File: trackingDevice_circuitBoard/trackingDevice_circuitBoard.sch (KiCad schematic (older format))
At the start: 17 parts, among them P1 Digital, P2 COM, P4 Analog, Q1 Q_NPN_EBC, Q2 Q_NPN_EBC, Q3 Q_NPN_EBC, U1 HC-12, U2 GY-NEO6MV2, U3 TP4056

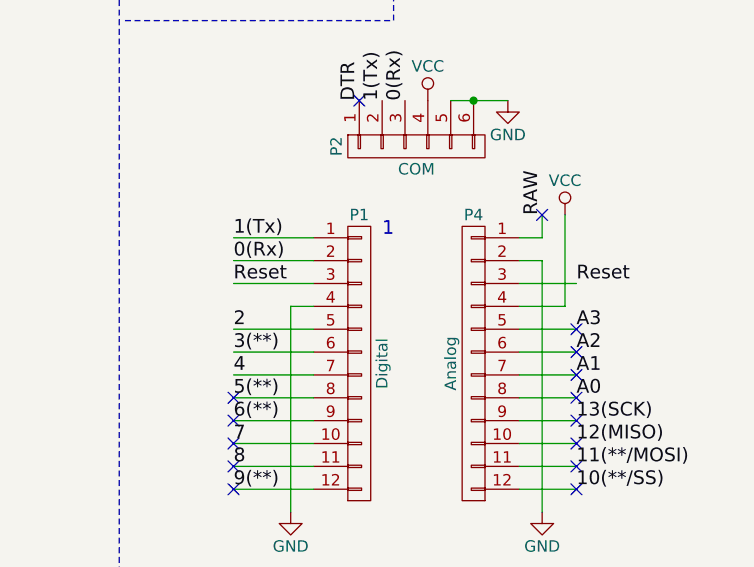
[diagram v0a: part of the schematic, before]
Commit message: Added veroboard/stripboard drill marks + corrected error in tracking device circuit
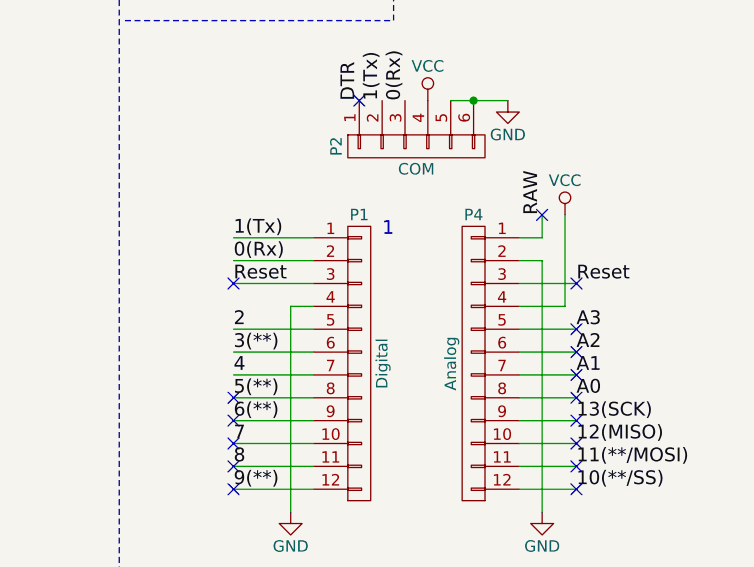
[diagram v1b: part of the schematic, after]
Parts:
- Q1: footprint TO_SOT_Packages_THT:TO-126_Vertical -> TO_SOT_Packages_THT:TO-92_Inline_Wide
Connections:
- no-connect marks 16 -> 18
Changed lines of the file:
@@
 Sheet 1 1
 Title "Arduino GPS Tracker - Tracking Device"
-Date "2018-07-16"
+Date "2018-08-09"
 Rev "1"
 Comp "By Megasaturnv"
@@
 F 0 "Q1" H 4500 2350 50  0000 L CNN
 F 1 "Q_NPN_EBC" H 4500 2250 50  0000 L CNN
-F 2 "TO_SOT_Packages_THT:TO-126_Vertical" H 4500 2400 50  0001 C CNN
+F 2 "TO_SOT_Packages_THT:TO-92_Inline_Wide" H 4500 2400 50  0001 C CNN
 F 3 "" H 4300 2300 50  0001 C CNN
 	1    4300 2300
@@
 	1    0    0    -1
 $EndComp
+NoConn ~ 10500 1800
+NoConn ~ 9000 1800
 $EndSCHEMATC

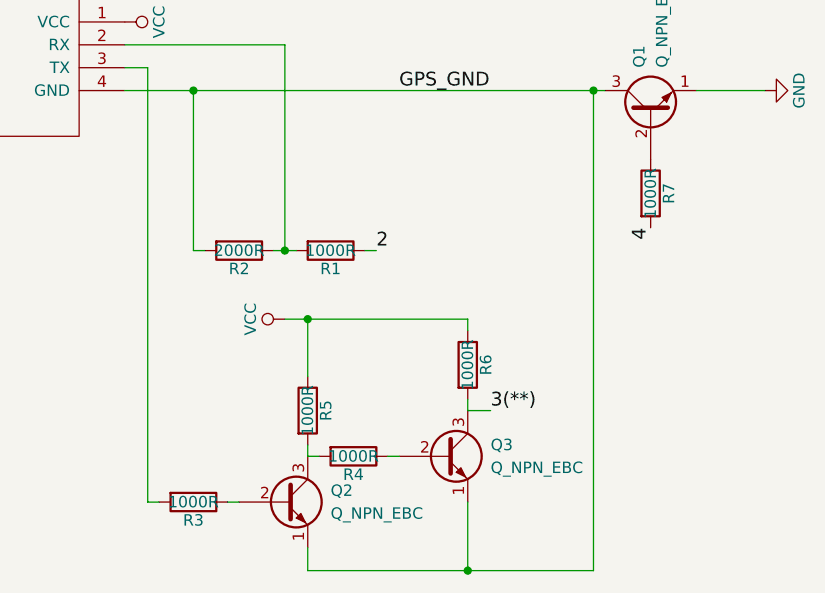
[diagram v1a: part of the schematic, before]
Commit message: Modified resistor values to be more power-efficient
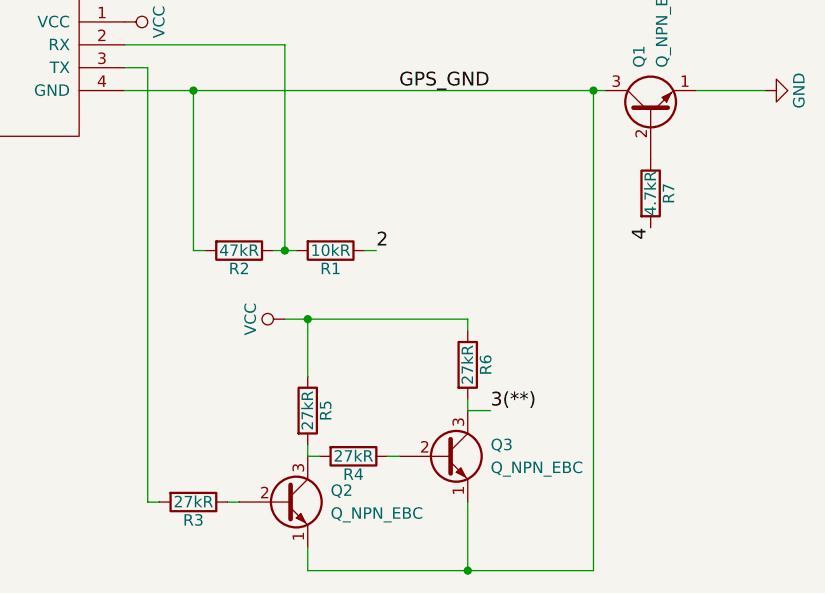
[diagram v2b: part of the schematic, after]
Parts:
- R1: value 1000R -> 10kR
- R2: value 2000R -> 47kR
- R3, R4, R5, R6: value 1000R -> 27kR
- R7: value 1000R -> 4.7kR
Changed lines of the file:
@@
 Sheet 1 1
 Title "Arduino GPS Tracker - Tracking Device"
-Date "2018-08-09"
+Date "2018-08-10"
 Rev "1"
 Comp "By Megasaturnv"
@@
 P 2900 2900
 F 0 "R1" V 2980 2900 50  0000 C CNN
-F 1 "1000R" V 2900 2900 50  0000 C CNN
+F 1 "10kR" V 2900 2900 50  0000 C CNN
 F 2 "Resistors_THT:R_Axial_DIN0207_L6.3mm_D2.5mm_P10.16mm_Horizontal" V 2830 2900 50  0001 C CNN
 F 3 "" H 2900 2900 50  0001 C CNN
@@
 P 2500 2900
 F 0 "R2" V 2580 2900 50  0000 C CNN
-F 1 "2000R" V 2500 2900 50  0000 C CNN
+F 1 "47kR" V 2500 2900 50  0000 C CNN
 F 2 "Resistors_THT:R_Axial_DIN0207_L6.3mm_D2.5mm_P10.16mm_Horizontal" V 2430 2900 50  0001 C CNN
 F 3 "" H 2500 2900 50  0001 C CNN
@@
 P 2300 4000
 F 0 "R3" V 2380 4000 50  0000 C CNN
-F 1 "1000R" V 2300 4000 50  0000 C CNN
+F 1 "27kR" V 2300 4000 50  0000 C CNN
 F 2 "Resistors_THT:R_Axial_DIN0207_L6.3mm_D2.5mm_P10.16mm_Horizontal" V 2230 4000 50  0001 C CNN
 F 3 "" H 2300 4000 50  0001 C CNN
@@
 P 3000 3800
 F 0 "R4" V 3080 3800 50  0000 C CNN
-F 1 "1000R" V 3000 3800 50  0000 C CNN
+F 1 "27kR" V 3000 3800 50  0000 C CNN
 F 2 "Resistors_THT:R_Axial_DIN0207_L6.3mm_D2.5mm_P10.16mm_Horizontal" V 2930 3800 50  0001 C CNN
 F 3 "" H 3000 3800 50  0001 C CNN
@@
 P 2800 3600
 F 0 "R5" V 2880 3600 50  0000 C CNN
-F 1 "1000R" V 2800 3600 50  0000 C CNN
+F 1 "27kR" V 2800 3600 50  0000 C CNN
 F 2 "Resistors_THT:R_Axial_DIN0207_L6.3mm_D2.5mm_P10.16mm_Horizontal" V 2730 3600 50  0001 C CNN
 F 3 "" H 2800 3600 50  0001 C CNN
@@
 P 3500 3400
 F 0 "R6" V 3580 3400 50  0000 C CNN
-F 1 "1000R" V 3500 3400 50  0000 C CNN
+F 1 "27kR" V 3500 3400 50  0000 C CNN
 F 2 "Resistors_THT:R_Axial_DIN0207_L6.3mm_D2.5mm_P10.16mm_Horizontal" V 3430 3400 50  0001 C CNN
 F 3 "" H 3500 3400 50  0001 C CNN
@@
 P 4300 2650
 F 0 "R7" V 4380 2650 50  0000 C CNN
-F 1 "1000R" V 4300 2650 50  0000 C CNN
+F 1 "4.7kR" V 4300 2650 50  0000 C CNN
 F 2 "Resistors_THT:R_Axial_DIN0207_L6.3mm_D2.5mm_P15.24mm_Horizontal" V 4230 2650 50  0001 C CNN
 F 3 "" H 4300 2650 50  0001 C CNN
